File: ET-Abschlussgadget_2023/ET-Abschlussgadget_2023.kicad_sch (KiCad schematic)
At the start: 22 parts, among them J1 PB0, J2 PB1, J3 UPDI / RESET, J4 EXTCLK, SW1 ON/OFF, U1 ATtiny414-SS

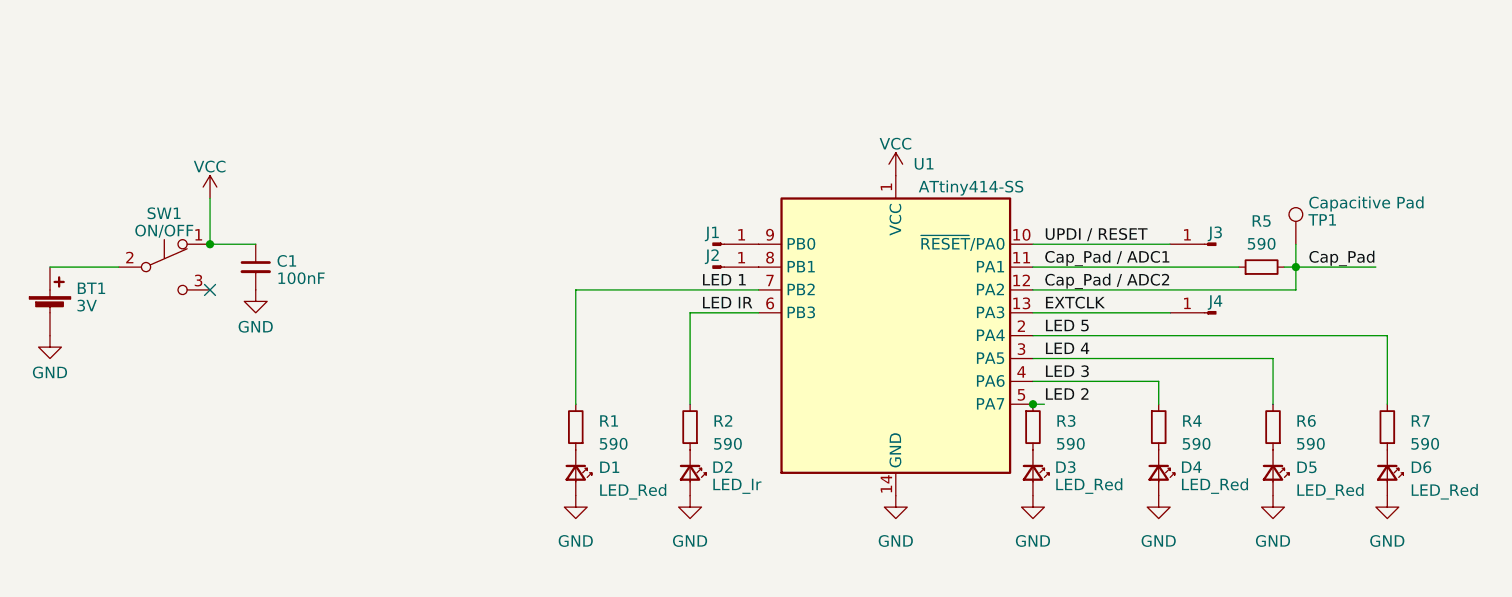
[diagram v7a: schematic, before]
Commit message: Redone whole layout based around new MCU, button and batteryholder-footprints are still placeholder tbd
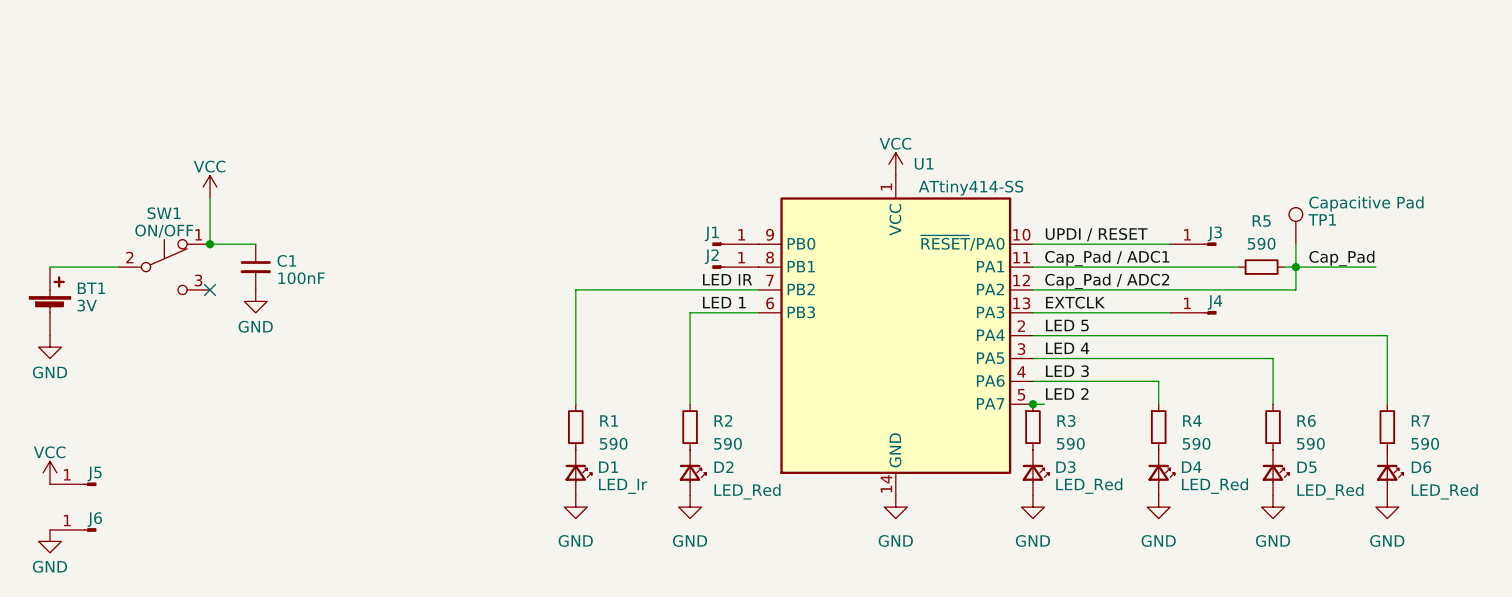
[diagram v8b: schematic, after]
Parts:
- added J5, J6: EXTCLK, TestPoint:TestPoint_Pad_D2.0mm, symbol Connector:Conn_01x01_Pin
- D1: value LED_Red -> LED_Ir; footprint LED_SMD:LED_0603_1608Metric -> LED_SMD:LED_1206_3216Metric
- D2: value LED_Ir -> LED_Red; footprint LED_SMD:LED_1206_3216Metric -> LED_SMD:LED_0603_1608Metric
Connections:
- net GND: now also J6.1 (Pin_1)
- net LED 1: now also R2.2, U1.6 (PB3); no longer R1.2, U1.7 (PB2)
- net LED IR: now also R1.2, U1.7 (PB2); no longer R2.2, U1.6 (PB3)
- net VCC: now also J5.1 (Pin_1)
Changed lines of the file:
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@@
+    (stroke (width 0) (type default))
+  )
+  (wire (pts (xy 128.27 90.17) (xy 135.89 90.17))
     (stroke (width 0) (type default))
   )
@@
     (stroke (width 0) (type default))
   )
-  (wire (pts (xy 128.27 90.17) (xy 135.89 90.17))
-    (stroke (width 0) (type default))
-  )
   (wire (pts (xy 166.37 95.25) (xy 193.04 95.25))
     (stroke (width 0) (type default))
@@
     (effects (font (size 1.27 1.27)) (justify left bottom))
   )
-  (label "LED 1" (at 129.54 87.63 0) (fields_autoplaced)
-    (effects (font (size 1.27 1.27)) (justify left bottom))
-  )
-  (label "LED IR" (at 129.54 90.17 0) (fields_autoplaced)
+  (label "LED 1" (at 129.54 90.17 0) (fields_autoplaced)
+    (effects (font (size 1.27 1.27)) (justify left bottom))
+  )
+  (label "LED IR" (at 129.54 87.63 0) (fields_autoplaced)
     (effects (font (size 1.27 1.27)) (justify left bottom))
   )
@@
         (path "/175a65ba-6b59-4269-bd86-2662d331b61e"
           (reference "#PWR04") (unit 1)
+        )
+      )
+    )
+  )
+  (symbol (lib_id "power:GND") (at 57.15 114.3 0) (unit 1)
+    (in_bom yes) (on_board yes) (dnp no) (fields_autoplaced)
+    (property "Reference" "#PWR013" (at 57.15 120.65 0)
+      (effects (font (size 1.27 1.27)) hide)
+    )
+    (property "Value" "GND" (at 57.15 118.4355 0)
+      (effects (font (size 1.27 1.27)))
+    )
+    (property "Footprint" "" (at 57.15 114.3 0)
+      (effects (font (size 1.27 1.27)) hide)
+    )
+    (property "Datasheet" "" (at 57.15 114.3 0)
+      (effects (font (size 1.27 1.27)) hide)
+    )
+    (pin "1")
+    (instances
+      (project "ET-Abschlussgadget_2023"
+        (path "/175a65ba-6b59-4269-bd86-2662d331b61e"
+          (reference "#PWR013") (unit 1)
         )
       )
@@
     )
   )
+  (symbol (lib_id "Device:LED_Small") (at 128.27 107.95 270) (unit 1)
+    (in_bom yes) (on_board yes) (dnp no) (fields_autoplaced)
+    (property "Reference" "D2" (at 130.81 107.3785 90)
+      (effects (font (size 1.27 1.27)) (justify left))
+    )
+    (property "Value" "LED_Red" (at 130.81 109.9185 90)
+      (effects (font (size 1.27 1.27)) (justify left))
+    )
+    (property "Footprint" "LED_SMD:LED_0603_1608Metric" (at 128.27 107.95 90)
+      (effects (font (size 1.27 1.27)) hide)
+    )
+    (property "Datasheet" "~" (at 128.27 107.95 90)
+      (effects (font (size 1.27 1.27)) hide)
+    )
+    (pin "1")
+    (pin "2")
+    (instances
+      (project "ET-Abschlussgadget_2023"
+        (path "/175a65ba-6b59-4269-bd86-2662d331b61e"
+          (reference "D2") (unit 1)
+        )
+      )
+    )
+  )
+  (symbol (lib_id "power:VCC") (at 57.15 109.22 0) (unit 1)
+    (in_bom yes) (on_board yes) (dnp no) (fields_autoplaced)
+    (property "Reference" "#PWR012" (at 57.15 113.03 0)
+      (effects (font (size 1.27 1.27)) hide)
+    )
+    (property "Value" "VCC" (at 57.15 105.7181 0)
+      (effects (font (size 1.27 1.27)))
+    )
+    (property "Footprint" "" (at 57.15 109.22 0)
+      (effects (font (size 1.27 1.27)) hide)
+    )
+    (property "Datasheet" "" (at 57.15 109.22 0)
+      (effects (font (size 1.27 1.27)) hide)
+    )
+    (pin "1")
+    (instances
+      (project "ET-Abschlussgadget_2023"
+        (path "/175a65ba-6b59-4269-bd86-2662d331b61e"
+          (reference "#PWR012") (unit 1)
+        )
+      )
+    )
+  )
   (symbol (lib_id "Device:LED_Small") (at 205.74 107.95 270) (unit 1)
     (in_bom yes) (on_board yes) (dnp no) (fields_autoplaced)
@@
     )
   )
+  (symbol (lib_id "Connector:Conn_01x01_Pin") (at 62.23 109.22 180) (unit 1)
+    (in_bom yes) (on_board yes) (dnp no)
+    (property "Reference" "J5" (at 62.23 107.95 0)
+      (effects (font (size 1.27 1.27)))
+    )
+    (property "Value" "EXTCLK" (at 49.53 107.95 0)
+      (effects (font (size 1.27 1.27)) (justify left) hide)
+    )
+    (property "Footprint" "TestPoint:TestPoint_Pad_D2.0mm" (at 62.23 109.22 0)
+      (effects (font (size 1.27 1.27)) hide)
+    )
+    (property "Datasheet" "~" (at 62.23 109.22 0)
+      (effects (font (size 1.27 1.27)) hide)
+    )
+    (pin "1")
+    (instances
+      (project "ET-Abschlussgadget_2023"
+        (path "/175a65ba-6b59-4269-bd86-2662d331b61e"
+          (reference "J5") (unit 1)
+        )
+      )
+    )
+  )
   (symbol (lib_id "power:VCC") (at 151.13 74.93 0) (unit 1)
     (in_bom yes) (on_board yes) (dnp no) (fields_autoplaced)
@@
     )
   )
-  (symbol (lib_id "Device:LED_Small") (at 115.57 107.95 270) (unit 1)
-    (in_bom yes) (on_board yes) (dnp no) (fields_autoplaced)
-    (property "Reference" "D1" (at 118.11 107.3785 90)
-      (effects (font (size 1.27 1.27)) (justify left))
-    )
-    (property "Value" "LED_Red" (at 118.11 109.9185 90)
-      (effects (font (size 1.27 1.27)) (justify left))
-    )
-    (property "Footprint" "LED_SMD:LED_0603_1608Metric" (at 115.57 107.95 90)
-      (effects (font (size 1.27 1.27)) hide)
-    )
-    (property "Datasheet" "~" (at 115.57 107.95 90)
-      (effects (font (size 1.27 1.27)) hide)
-    )
-    (pin "1")
-    (pin "2")
-    (instances
-      (project "ET-Abschlussgadget_2023"
-        (path "/175a65ba-6b59-4269-bd86-2662d331b61e"
-          (reference "D1") (unit 1)
-        )
-      )
-    )
-  )
   (symbol (lib_id "power:GND") (at 166.37 110.49 0) (unit 1)
     (in_bom yes) (on_board yes) (dnp no) (fields_autoplaced)
@@
         (path "/175a65ba-6b59-4269-bd86-2662d331b61e"
           (reference "#PWR08") (unit 1)
+        )
+      )
+    )
+  )
+  (symbol (lib_id "Connector:Conn_01x01_Pin") (at 62.23 114.3 180) (unit 1)
+    (in_bom yes) (on_board yes) (dnp no)
+    (property "Reference" "J6" (at 62.23 113.03 0)
+      (effects (font (size 1.27 1.27)))
+    )
+    (property "Value" "EXTCLK" (at 49.53 113.03 0)
+      (effects (font (size 1.27 1.27)) (justify left) hide)
+    )
+    (property "Footprint" "TestPoint:TestPoint_Pad_D2.0mm" (at 62.23 114.3 0)
+      (effects (font (size 1.27 1.27)) hide)
+    )
+    (property "Datasheet" "~" (at 62.23 114.3 0)
+      (effects (font (size 1.27 1.27)) hide)
+    )
+    (pin "1")
+    (instances
+      (project "ET-Abschlussgadget_2023"
+        (path "/175a65ba-6b59-4269-bd86-2662d331b61e"
+          (reference "J6") (unit 1)
         )
       )
@@
     )
   )
-  (symbol (lib_id "Device:LED_Small") (at 128.27 107.95 270) (unit 1)
-    (in_bom yes) (on_board yes) (dnp no) (fields_autoplaced)
-    (property "Reference" "D2" (at 130.683 107.3698 90)
-      (effects (font (size 1.27 1.27)) (justify left))
-    )
-    (property "Value" "LED_Ir" (at 130.683 109.2908 90)
-      (effects (font (size 1.27 1.27)) (justify left))
-    )
-    (property "Footprint" "LED_SMD:LED_1206_3216Metric" (at 128.27 107.95 90)
-      (effects (font (size 1.27 1.27)) hide)
-    )
-    (property "Datasheet" "~" (at 128.27 107.95 90)
-      (effects (font (size 1.27 1.27)) hide)
-    )
-    (pin "1")
-    (pin "2")
-    (instances
-      (project "ET-Abschlussgadget_2023"
-        (path "/175a65ba-6b59-4269-bd86-2662d331b61e"
-          (reference "D2") (unit 1)
-        )
-      )
-    )
-  )
   (symbol (lib_id "Connector:Conn_01x01_Pin") (at 130.81 82.55 0) (unit 1)
     (in_bom yes) (on_board yes) (dnp no)
@@
         )
       )
+    )
+  )
+  (symbol (lib_id "Device:LED_Small") (at 115.57 107.95 270) (unit 1)
+    (in_bom yes) (on_board yes) (dnp no) (fields_autoplaced)
+    (property "Reference" "D1" (at 117.983 107.3698 90)
+      (effects (font (size 1.27 1.27)) (justify left))
+    )
+    (property "Value" "LED_Ir" (at 117.983 109.2908 90)
+      (effects (font (size 1.27 1.27)) (justify left))
+    )
+    (property "Footprint" "LED_SMD:LED_1206_3216Metric" (at 115.57 107.95 90)
+      (effects (font (size 1.27 1.27)) hide)
+    )
+    (property "Datasheet" "~" (at 115.57 107.95 90)
+      (effects (font (size 1.27 1.27)) hide)
+    )
+    (pin "1")
+    (pin "2")
+    (instances
+      (project "ET-Abschlussgadget_2023"
+        (path "/175a65ba-6b59-4269-bd86-2662d331b61e"
+          (reference "D1") (unit 1)
+        )
+      )
